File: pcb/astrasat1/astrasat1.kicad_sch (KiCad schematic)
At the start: 17 parts, among them M1 Motor_Servo, SW1 SW_SPDT, U2 MPU-6050, U7 DS1302+, U9 Pico, Y1 Crystal

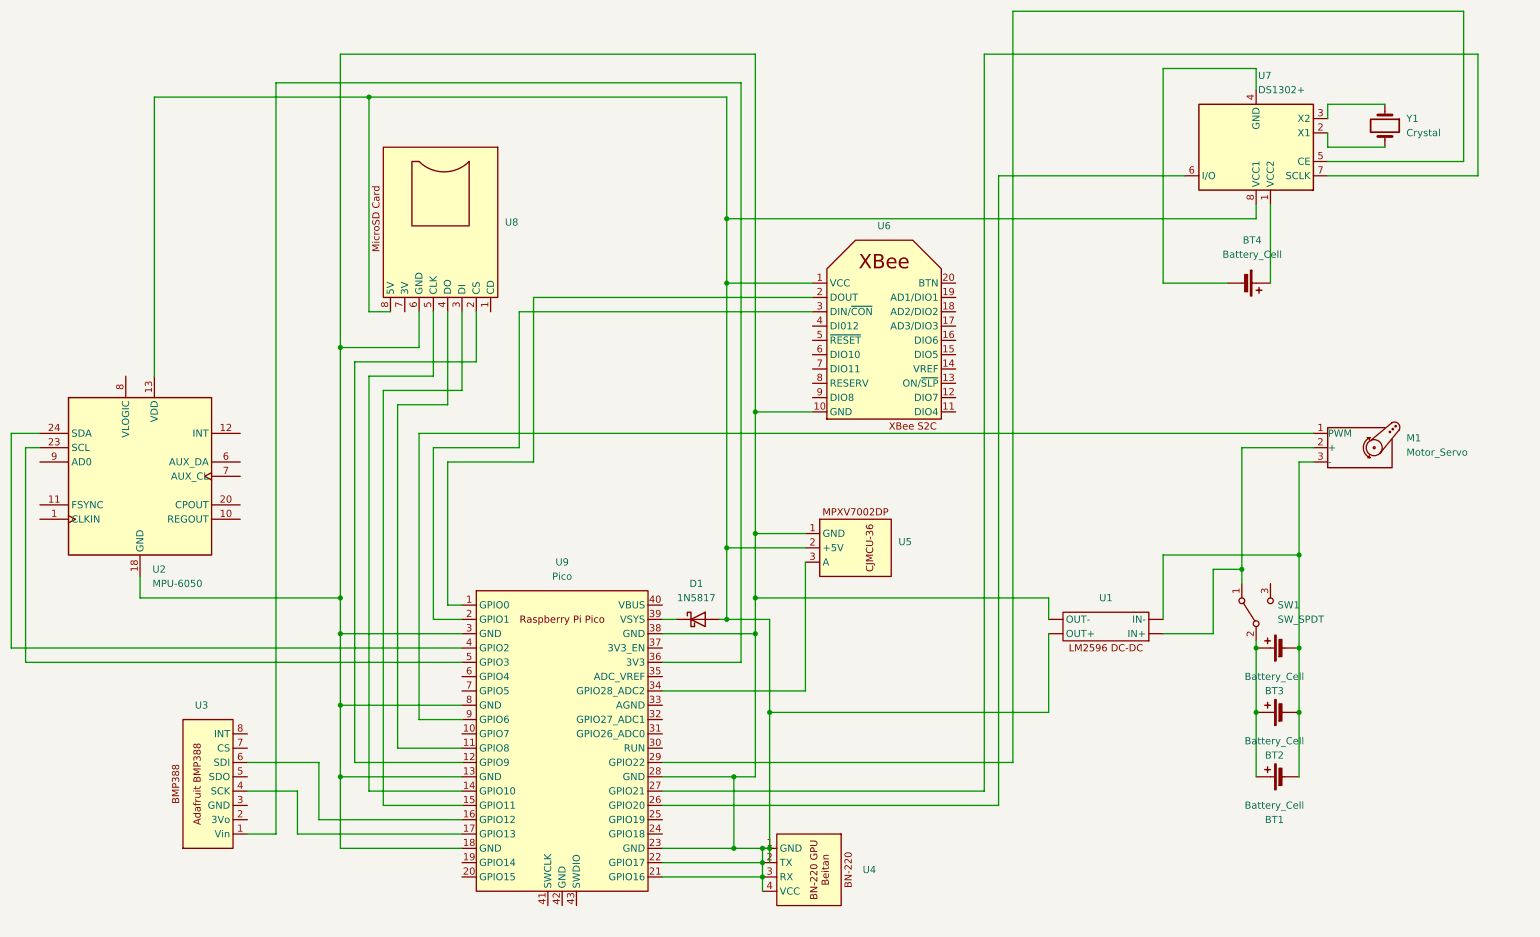
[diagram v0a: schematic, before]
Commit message: add new schematic and some custom footprints
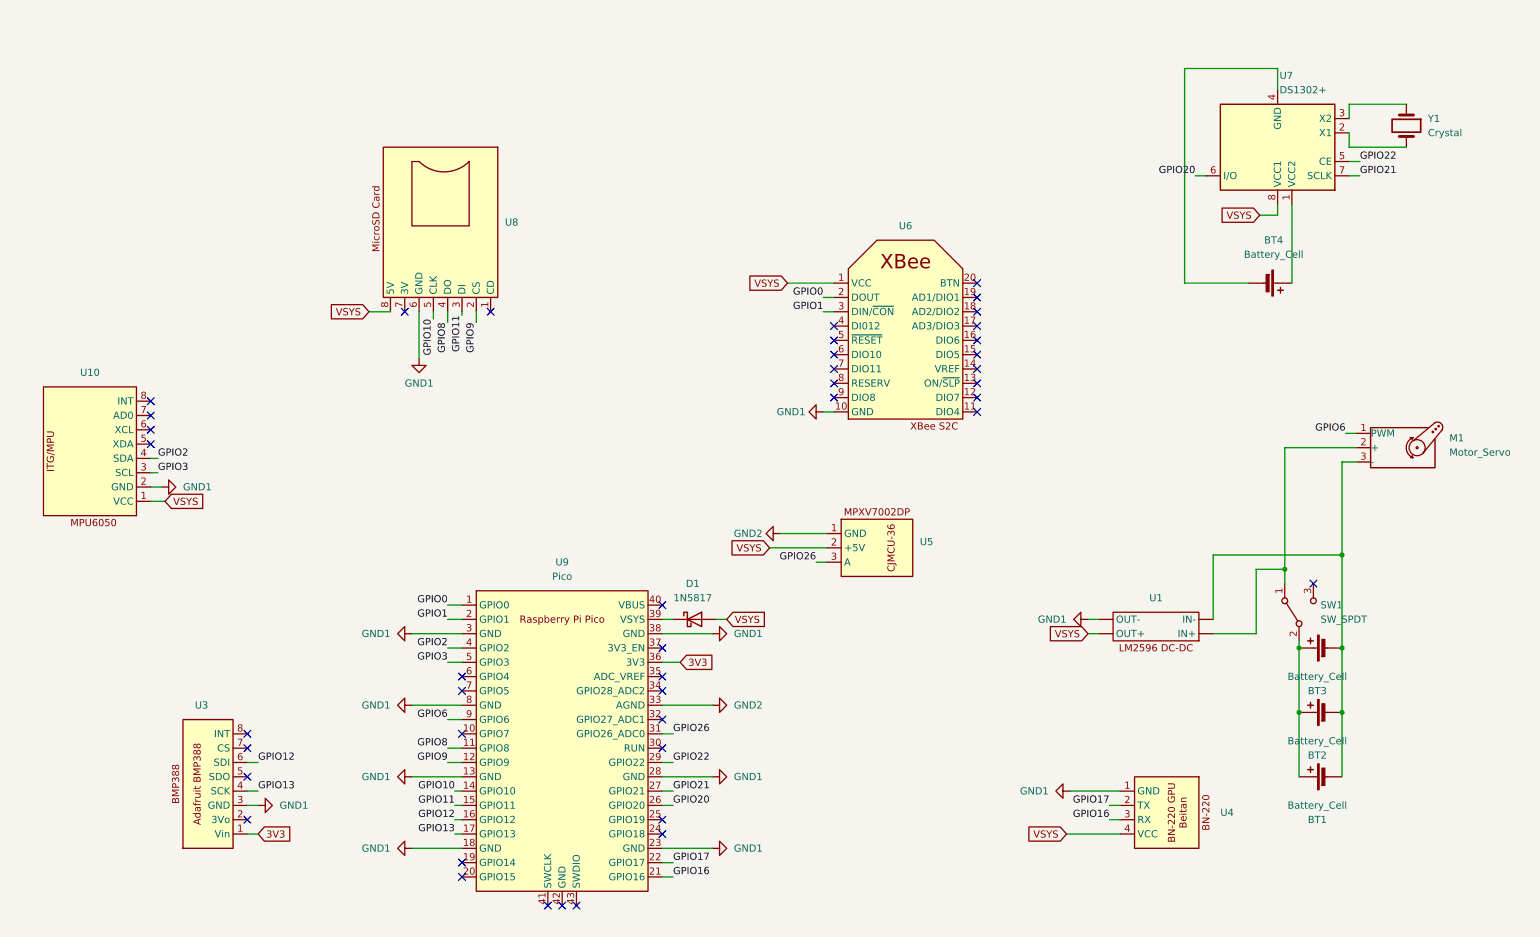
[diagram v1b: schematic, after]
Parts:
- removed U2: MPU-6050, Sensor_Motion:InvenSense_QFN-24_4x4mm_P0.5mm, symbol Sensor_Motion:MPU-6050
- added U10: ~, symbol CansatParts:MPU6050_ITG/MPU
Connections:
- net GPIO6: now reaches M1.1 (PWM), U9.9 (GPIO6)
- net GPIO9: now reaches U8.2 (CS), U9.12 (GPIO9)
- net GPIO11: now reaches U8.3 (DI), U9.15 (GPIO11)
- net GPIO8: now reaches U8.4 (DO), U9.11 (GPIO8)
- net GPIO10: now reaches U8.5 (CLK), U9.14 (GPIO10)
- net GPIO0: now reaches U6.2 (DOUT), U9.1 (GPIO0)
- net GPIO1: now reaches U6.3 (DIN/~{CON}), U9.2 (GPIO1)
- net GPIO12: now reaches U3.6 (SDI), U9.16 (GPIO12)
- net GPIO13: now reaches U3.4 (SCK), U9.17 (GPIO13)
- net GPIO20: now reaches U7.6 (I/O), U9.26 (GPIO20)
- net GPIO21: now reaches U7.7 (SCLK), U9.27 (GPIO21)
- net GPIO22: now reaches U7.5 (CE), U9.29 (GPIO22)
- net GPIO26: now reaches U9.31 (GPIO26_ADC0)
- net GPIO26: now also U5.3 (A)
- net GND2: now reaches U9.33 (AGND)
- net GND2: now also U5.1 (GND)
- net at U9.34 (GPIO28_ADC2): no longer U5.3 (A)
- net 3V3: now reaches U3.1 (Vin), U9.36 (3V3)
- net GPIO2: now reaches U9.4 (GPIO2)
- net GPIO2: now also U10.4 (SDA)
- net GPIO3: now reaches U9.5 (GPIO3)
- net GPIO3: now also U10.3 (SCL)
- net GND1: now reaches U3.3 (GND)
- net GND1: now also U1. (OUT-), U4.1 (GND), U6.10 (GND), U8.6 (GND), U9.13 (GND), U9.18 (GND), U9.23 (GND), U9.28 (GND), U9.3 (GND), U9.38 (GND), U9.8 (GND), U10.2 (GND)
- new net GPIO16: U4.3 (RX), U9.21 (GPIO16)
- new net GPIO17: U4.2 (TX), U9.22 (GPIO17)
- new net VSYS: D1.2 (A), U1. (OUT-), U10.1 (VCC), U4.4 (VCC), U5.2 (+5V), U6.1 (VCC), U7.8 (VCC1), U8.8 (5V)
- no-connect marks 0 -> 43
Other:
- moved on the sheet: BT1, BT2, BT3, BT4, D1, M1, SW1, U1, U4, U5, U6, U7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

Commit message: edit schematic, complete all footprints and annotate them with the symbols
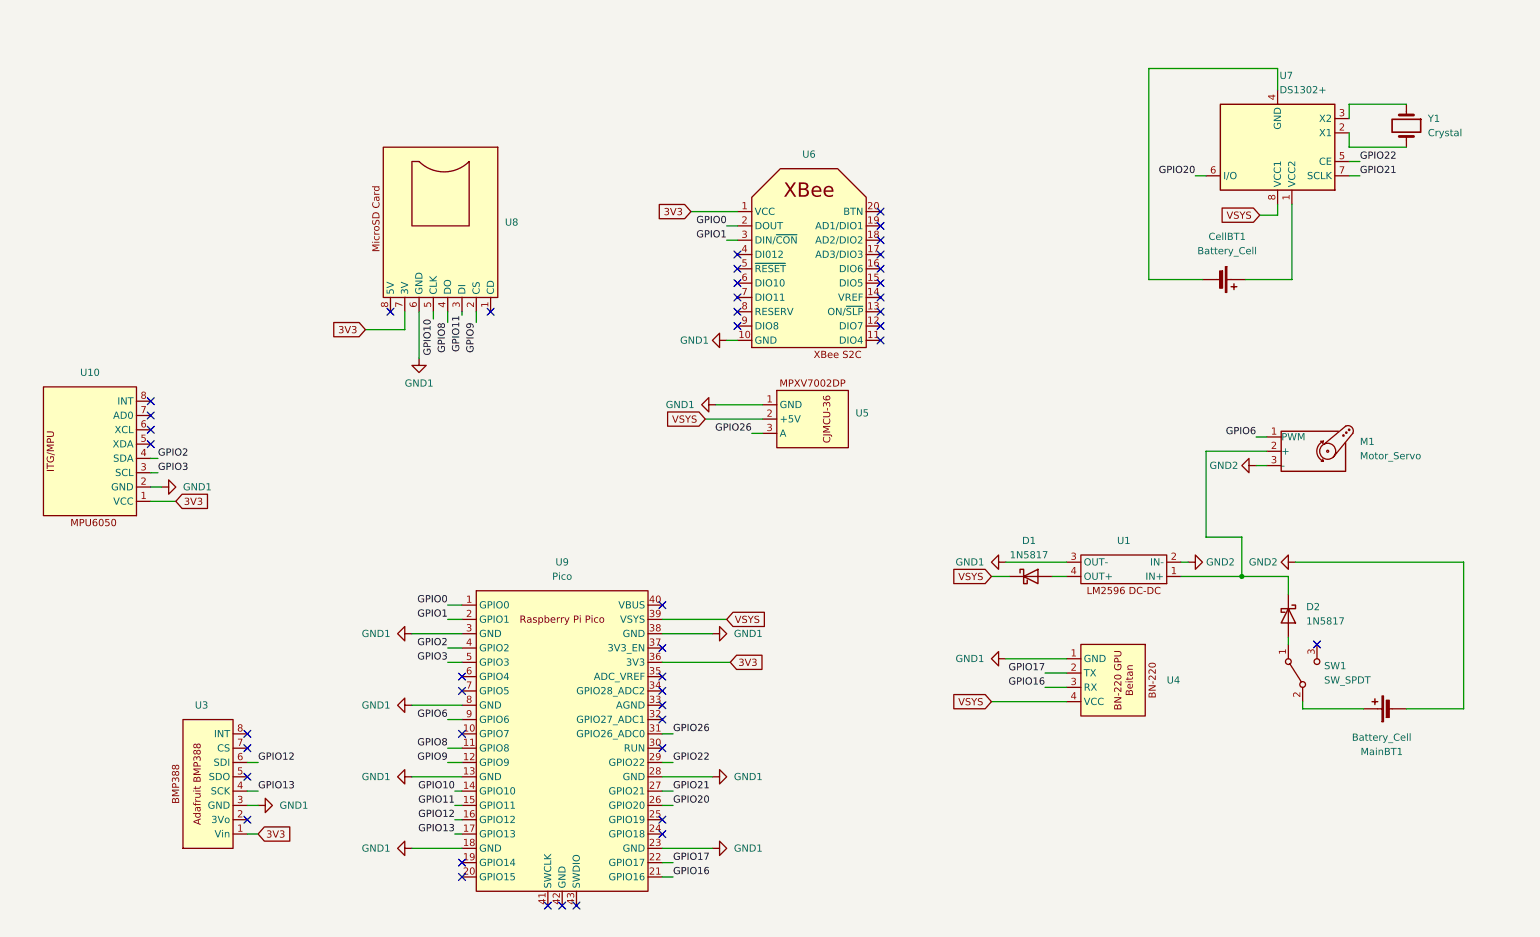
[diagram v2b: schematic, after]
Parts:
- removed BT1, BT3: Battery_Cell, symbol Device:Battery_Cell
- added D2: 1N5817, Diode_THT:D_DO-41_SOD81_P10.16mm_Horizontal, symbol Diode:1N5817
- CellBT1: renamed from BT4; footprint (none) -> Battery:BatteryHolder_Keystone_103_1x20mm
- MainBT1: renamed from BT2; footprint (none) -> Connector_PinHeader_2.54mm:PinHeader_1x02_P2.54mm_Vertical
- SW1: footprint (none) -> Button_Switch_THT:SW_E-Switch_EG1271_SPDT
- U1: footprint (none) -> CansatFootprints:LM2596 Voltage Regulator board
- U10: footprint (none) -> CansatFootprints:MPU6050 Module
- U3: footprint (none) -> CansatFootprints:Adafruit BMP388 Blue
- U4: footprint (none) -> CansatFootprints:BN-220
- U5: footprint (none) -> Connector_PinHeader_2.54mm:PinHeader_1x03_P2.54mm_Vertical
- U6: footprint (none) -> CansatFootprints:XBee S2C
- U8: footprint (none) -> CansatFootprints:Adafruit MicroSD Breakout
- U9: footprint RPi_Pico:RPi_Pico_SMD_TH -> MCU_RaspberryPi_and_Boards:RPi_Pico_SMD_TH
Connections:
- net 3V3: now also U10.1 (VCC), U6.1 (VCC), U8.7 (3V)
- net GND1: now also U1.3 (OUT-), U5.1 (GND); no longer U1. (OUT-)
- net GND2: now also M1.3 (-), MainBT1.2 (-), U1.2 (IN-); no longer U5.1 (GND), U9.33 (AGND)
- net VSYS: now also D1.1 (K), U9.39 (VSYS); no longer D1.2 (A), U1. (OUT-), U10.1 (VCC), U6.1 (VCC), U8.8 (5V)
- new net: D2.1 (K), M1.2 (+), U1.1 (IN+)
- new net: D2.2 (A), SW1.1 (A)
- new net: D1.2 (A), U1.4 (OUT+)
- no-connect marks 43 -> 44
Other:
- moved on the sheet: CellBT1, M1, MainBT1, SW1, U4, U5, U6

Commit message: add pcb and 3d files
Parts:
- added SmallM1: Motor_Servo, Connector_PinHeader_2.54mm:PinHeader_1x03_P2.54mm_Vertical, symbol Motor:Motor_Servo
- D1, D2: footprint Diode_THT:D_DO-41_SOD81_P10.16mm_Horizontal -> Diode_THT:D_DO-41_SOD81_P7.62mm_Horizontal
- renumbered M1 to BigM1, U4 to U1, U5 to U2, U7 to U3, U6 to U4, U9 to U5, U8 to U6, U3 to U7, U10 to U8, U1 to U9
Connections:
- net GND1: now also SmallM1.3 (-)
- net VSYS: now also SmallM1.2 (+)
- net GPIO7: now reaches U5.10 (GPIO7)
- net GPIO7: now also SmallM1.1 (PWM)
- no-connect marks 44 -> 43
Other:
- company: ASTRA Team - Politecnico di Torino -> (none)
- moved on the sheet: CellBT1, U1, U2, U3, U4, U5, U6, U7, U8, Y1
